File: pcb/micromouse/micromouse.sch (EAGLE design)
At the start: 55 parts, among them J1 Connector_M1, J2 Connector_M2, J4 Programmer

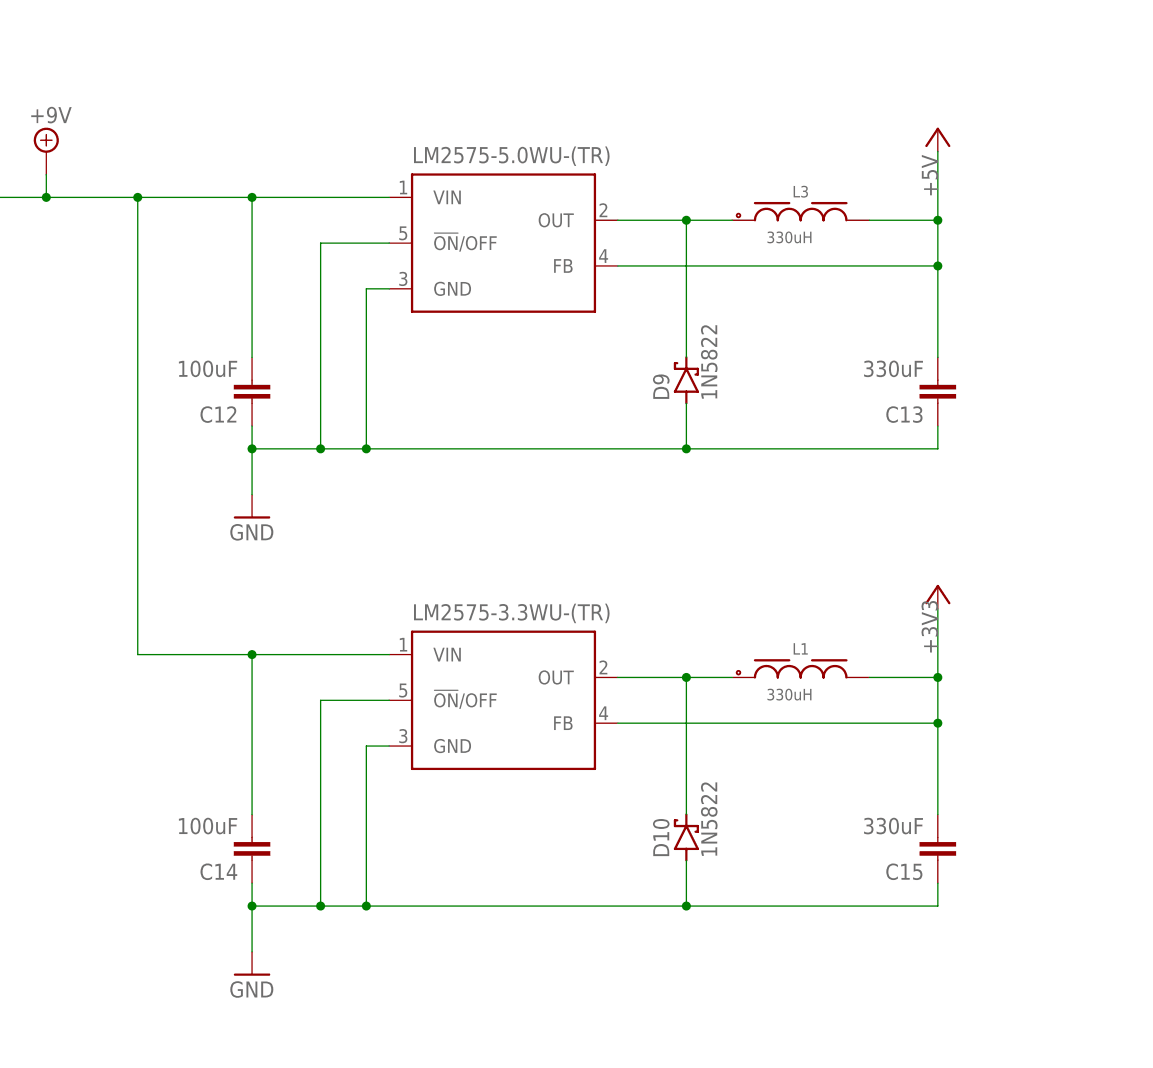
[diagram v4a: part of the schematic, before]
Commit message: Exchanged capacitors and inductances in power supply
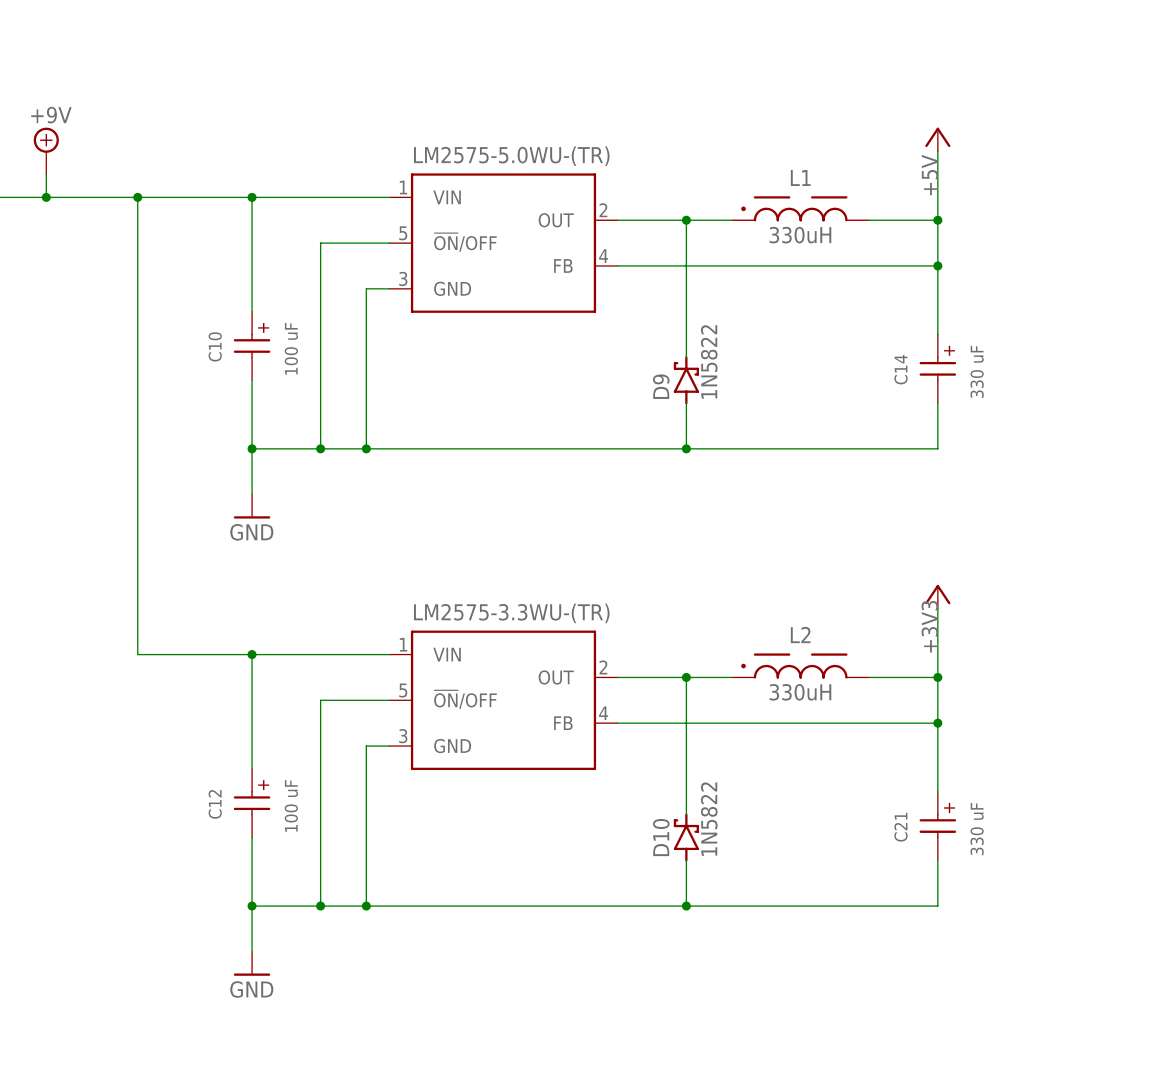
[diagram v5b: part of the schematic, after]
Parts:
- removed C13, C15: 330uF, rcl:C-EUC0805
- removed L3: 330uH, Eagle_WE-PD (rev20a):WE-PD_1210_7447709331
- added C10: 100 uF, Eagle_WCAP-ATG5 (rev21a):WCAP-ATG5_5X11_860020272005
- added C21: 330 uF, Eagle_WCAP-ATG5 (rev21a):WCAP-ATG5_6.3X11_860020273010
- added L2: 330uH, Eagle_WE-TIS (rev22a):WE-TIS_1111_7447471331
- C12: value 100uF -> 100 uF; device rcl:C-EUC1210 -> Eagle_WCAP-ATG5 (rev21a):WCAP-ATG5_5X11_860020272005
- C14: value 100uF -> 330 uF; device rcl:C-EUC1210 -> Eagle_WCAP-ATG5 (rev21a):WCAP-ATG5_6.3X11_860020273010
- L1: device Eagle_WE-PD (rev20a):WE-PD_1210_7447709331 -> Eagle_WE-TIS (rev22a):WE-TIS_1111_7447471331
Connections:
- net +3V3: now also C21.+, L2.2; no longer C15.2, L1.2
- net +5V: now also C14.+, L1.2; no longer C13.2, L3.2
- net +9V: now also C10.+, C12.+; no longer C12.2, C14.2
- net GND: now also C10.-, C12.-, C14.-, C21.-; no longer C12.1, C13.1, C14.1, C15.1
- net N$7: now also L1.1; no longer L3.1
- net N$8: now also L2.1; no longer L1.1
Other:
- moved on the sheet: L1

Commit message: Add test points
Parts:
- added 3V3_TEST, 5V_TEST, 9V_TEST, AVDD_TEST, AVSS_TEST1, GND_TEST, IR0_TEST, IR1_TEST, IR2_TEST, PWM1L1_TEST, PWM1L2_TEST: (no value), wirepad:3,17/1,3
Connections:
- net +3V3: now also 3V3_TEST.P
- net +5V: now also 5V_TEST.P
- net +9V: now also 9V_TEST.P
- net AVDD: now also AVDD_TEST.P
- net AVSS: now also AVSS_TEST1.P
- net GND: now also GND_TEST.P
- net IR0: now also IR0_TEST.P
- net IR1: now also IR1_TEST.P
- net IR2: now also IR2_TEST.P
- net PWM1L1: now also PWM1L1_TEST.P
- net PWM1L2: now also PWM1L2_TEST.P
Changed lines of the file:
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@@
 <part name="L1" library="Eagle_WE-TIS (rev22a)" deviceset="WE-TIS_1111" device="" package3d_urn="urn:adsk.eagle:package:12988462/4" technology="_7447471331" value="330uH"/>
 <part name="L2" library="Eagle_WE-TIS (rev22a)" deviceset="WE-TIS_1111" device="" package3d_urn="urn:adsk.eagle:package:12988462/4" technology="_7447471331" value="330uH"/>
+<part name="9V_TEST" library="wirepad" library_urn="urn:adsk.eagle:library:412" deviceset="3,17/1,3" device="" package3d_urn="urn:adsk.eagle:package:30833/1"/>
+<part name="5V_TEST" library="wirepad" library_urn="urn:adsk.eagle:library:412" deviceset="3,17/1,3" device="" package3d_urn="urn:adsk.eagle:package:30833/1"/>
+<part name="3V3_TEST" library="wirepad" library_urn="urn:adsk.eagle:library:412" deviceset="3,17/1,3" device="" package3d_urn="urn:adsk.eagle:package:30833/1"/>
+<part name="IR0_TEST" library="wirepad" library_urn="urn:adsk.eagle:library:412" deviceset="3,17/1,3" device="" package3d_urn="urn:adsk.eagle:package:30833/1"/>
+<part name="IR1_TEST" library="wirepad" library_urn="urn:adsk.eagle:library:412" deviceset="3,17/1,3" device="" package3d_urn="urn:adsk.eagle:package:30833/1"/>
+<part name="IR2_TEST" library="wirepad" library_urn="urn:adsk.eagle:library:412" deviceset="3,17/1,3" device="" package3d_urn="urn:adsk.eagle:package:30833/1"/>
+<part name="AVDD_TEST" library="wirepad" library_urn="urn:adsk.eagle:library:412" deviceset="3,17/1,3" device="" package3d_urn="urn:adsk.eagle:package:30833/1"/>
+<part name="PWM1L2_TEST" library="wirepad" library_urn="urn:adsk.eagle:library:412" deviceset="3,17/1,3" device="" package3d_urn="urn:adsk.eagle:package:30833/1"/>
+<part name="PWM1L1_TEST" library="wirepad" library_urn="urn:adsk.eagle:library:412" deviceset="3,17/1,3" device="" package3d_urn="urn:adsk.eagle:package:30833/1"/>
+<part name="GND_TEST" library="wirepad" library_urn="urn:adsk.eagle:library:412" deviceset="3,17/1,3" device="" package3d_urn="urn:adsk.eagle:package:30833/1"/>
+<part name="AVSS_TEST1" library="wirepad" library_urn="urn:adsk.eagle:library:412" deviceset="3,17/1,3" device="" package3d_urn="urn:adsk.eagle:package:30833/1"/>
 </parts>
 <sheets>
@@
 <attribute name="NAME" x="10.16" y="295.91" size="1.778" layer="95" align="bottom-center"/>
 <attribute name="VALUE" x="10.16" y="289.56" size="1.778" layer="96" align="bottom-center"/>
+</instance>
+<instance part="9V_TEST" gate="1" x="-73.66" y="342.9" smashed="yes" rot="R90">
+<attribute name="NAME" x="-75.5142" y="334.137" size="1.778" layer="95" rot="R90"/>
+<attribute name="VALUE" x="-70.358" y="341.757" size="1.778" layer="96" rot="R90"/>
+</instance>
+<instance part="5V_TEST" gate="1" x="27.94" y="342.9" smashed="yes" rot="R180">
+<attribute name="NAME" x="36.703" y="341.0458" size="1.778" layer="95" rot="R180"/>
+<attribute name="VALUE" x="29.083" y="346.202" size="1.778" layer="96" rot="R180"/>
+</instance>
+<instance part="3V3_TEST" gate="1" x="27.94" y="292.1" smashed="yes" rot="R180">
+<attribute name="NAME" x="39.243" y="290.2458" size="1.778" layer="95" rot="R180"/>
+<attribute name="VALUE" x="29.083" y="295.402" size="1.778" layer="96" rot="R180"/>
+</instance>
+<instance part="IR0_TEST" gate="1" x="147.32" y="309.88" smashed="yes" rot="R180">
+<attribute name="NAME" x="156.083" y="308.0258" size="1.778" layer="95" rot="R180"/>
+<attribute name="VALUE" x="148.463" y="313.182" size="1.778" layer="96" rot="R180"/>
+</instance>
+<instance part="IR1_TEST" gate="1" x="147.32" y="292.1" smashed="yes" rot="R180">
+<attribute name="NAME" x="156.083" y="290.2458" size="1.778" layer="95" rot="R180"/>
+<attribute name="VALUE" x="148.463" y="295.402" size="1.778" layer="96" rot="R180"/>
+</instance>
+<instance part="IR2_TEST" gate="1" x="147.32" y="274.32" smashed="yes" rot="R180">
+<attribute name="NAME" x="156.083" y="272.4658" size="1.778" layer="95" rot="R180"/>
+<attribute name="VALUE" x="148.463" y="277.622" size="1.778" layer="96" rot="R180"/>
+</instance>
+<instance part="AVDD_TEST" gate="1" x="154.94" y="66.04" smashed="yes" rot="R180">
+<attribute name="NAME" x="163.703" y="64.1858" size="1.778" layer="95" rot="R180"/>
+<attribute name="VALUE" x="156.083" y="69.342" size="1.778" layer="96" rot="R180"/>
+</instance>
+<instance part="PWM1L2_TEST" gate="1" x="58.42" y="134.62" smashed="yes">
+<attribute name="NAME" x="42.037" y="136.4742" size="1.778" layer="95"/>
+<attribute name="VALUE" x="57.277" y="131.318" size="1.778" layer="96"/>
+</instance>
+<instance part="PWM1L1_TEST" gate="1" x="58.42" y="124.46" smashed="yes">
+<attribute name="NAME" x="42.037" y="126.3142" size="1.778" layer="95"/>
+<attribute name="VALUE" x="57.277" y="121.158" size="1.778" layer="96"/>
+</instance>
+<instance part="GND_TEST" gate="1" x="-86.36" y="340.36" smashed="yes" rot="R180">
+<attribute name="NAME" x="-82.677" y="343.5858" size="1.778" layer="95" rot="R180"/>
+<attribute name="VALUE" x="-85.217" y="343.662" size="1.778" layer="96" rot="R180"/>
+</instance>
+<instance part="AVSS_TEST1" gate="1" x="154.94" y="53.34" smashed="yes" rot="R180">
+<attribute name="NAME" x="163.703" y="51.4858" size="1.778" layer="95" rot="R180"/>
+<attribute name="VALUE" x="156.083" y="56.642" size="1.778" layer="96" rot="R180"/>
 </instance>
 </instances>
@@
 <wire x1="-88.9" y1="340.36" x2="-88.9" y2="335.28" width="0.1524" layer="91"/>
 <pinref part="SV5" gate="G$1" pin="1"/>
+<pinref part="GND_TEST" gate="1" pin="P"/>
+<junction x="-88.9" y="340.36"/>
 </segment>
 <segment>
@@
 <pinref part="R14" gate="G$1" pin="2"/>
 <pinref part="C9" gate="G$1" pin="2"/>
+<pinref part="AVDD_TEST" gate="1" pin="P"/>
 </segment>
 </net>
@@
 <junction x="25.4" y="287.02"/>
 <pinref part="L2" gate="G$1" pin="2"/>
+<pinref part="3V3_TEST" gate="1" pin="P"/>
 </segment>
 <segment>
@@
 <pinref part="R13" gate="G$1" pin="2"/>
 <pinref part="C9" gate="G$1" pin="1"/>
+<pinref part="AVSS_TEST1" gate="1" pin="P"/>
 </segment>
 </net>
@@
 <junction x="25.4" y="337.82"/>
 <pinref part="L1" gate="G$1" pin="2"/>
+<pinref part="5V_TEST" gate="1" pin="P"/>
 </segment>
 <segment>
@@
 <wire x1="111.76" y1="274.32" x2="144.78" y2="274.32" width="0.1524" layer="91"/>
 <label x="139.7" y="274.32" size="1.778" layer="95"/>
+<pinref part="IR2_TEST" gate="1" pin="P"/>
 </segment>
 </net>
@@
 <pinref part="C10" gate="G$1" pin="+"/>
 <pinref part="C12" gate="G$1" pin="+"/>
+<pinref part="9V_TEST" gate="1" pin="P"/>
 </segment>
 </net>
@@
 <wire x1="71.12" y1="124.46" x2="60.96" y2="124.46" width="0.1524" layer="91"/>
 <label x="60.96" y="124.46" size="1.778" layer="95"/>
+<pinref part="PWM1L1_TEST" gate="1" pin="P"/>
 </segment>
 <segment>
@@
 <wire x1="71.12" y1="134.62" x2="60.96" y2="134.62" width="0.1524" layer="91"/>
 <label x="60.96" y="134.62" size="1.778" layer="95"/>
+<pinref part="PWM1L2_TEST" gate="1" pin="P"/>
 </segment>
 <segment>
@@
 <wire x1="111.76" y1="309.88" x2="144.78" y2="309.88" width="0.1524" layer="91"/>
 <label x="139.7" y="309.88" size="1.778" layer="95"/>
+<pinref part="IR0_TEST" gate="1" pin="P"/>
 </segment>
 </net>
@@
 <wire x1="111.76" y1="292.1" x2="144.78" y2="292.1" width="0.1524" layer="91"/>
 <label x="139.7" y="292.1" size="1.778" layer="95"/>
-</segment>
-</net>
+<pinref part="IR1_TEST" gate="1" pin="P"/>
+</segment>
+</net>

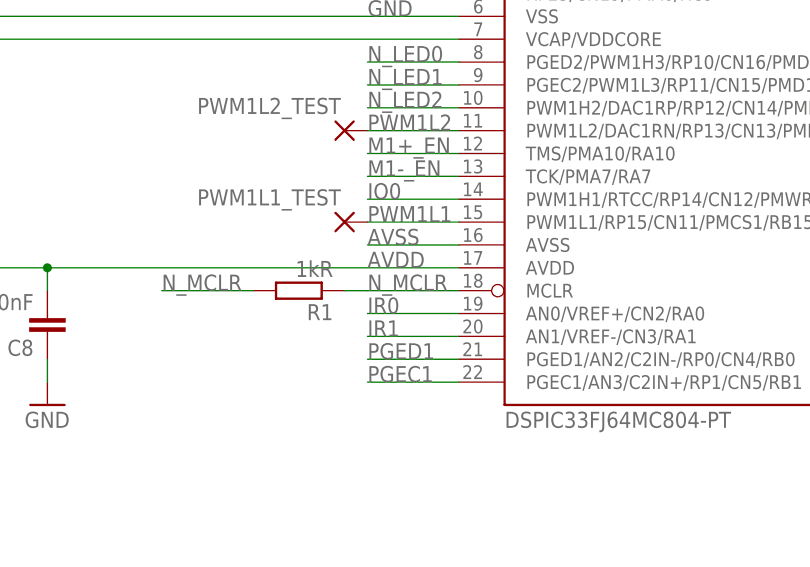
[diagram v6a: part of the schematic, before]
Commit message: Increase width of lanes, all 45 degree angles errors resolved design rules obeyed
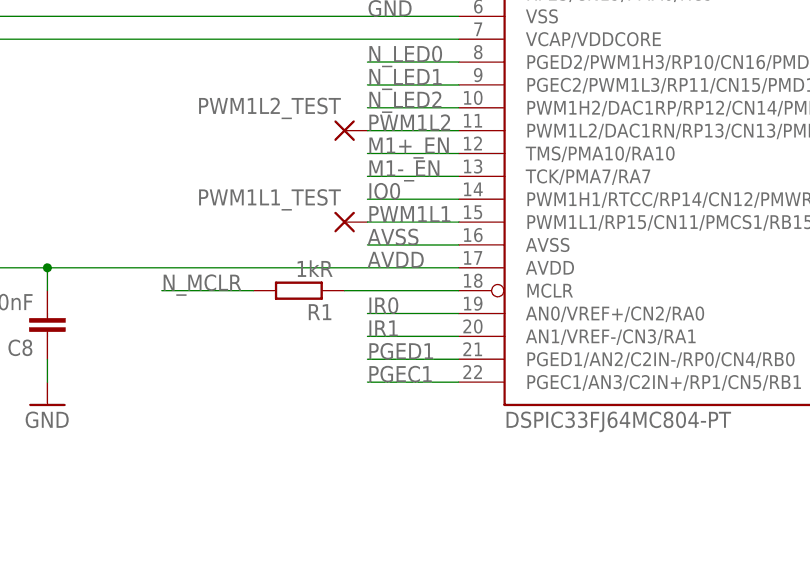
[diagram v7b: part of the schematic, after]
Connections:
- new net N$1: MICROCONTROLLER.MCLR, R1.1
- net N_MCLR: no longer MICROCONTROLLER.MCLR, R1.1
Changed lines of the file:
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@@
-</segment>
-<segment>
-<wire x1="71.12" y1="116.84" x2="63.5" y2="116.84" width="0.1524" layer="91"/>
-<label x="60.96" y="116.84" size="1.778" layer="95"/>
-<pinref part="MICROCONTROLLER" gate="G$1" pin="MCLR"/>
-<pinref part="R1" gate="G$1" pin="1"/>
-<wire x1="63.5" y1="116.84" x2="60.96" y2="116.84" width="0.1524" layer="91"/>
-<wire x1="58.42" y1="116.84" x2="60.96" y2="116.84" width="0.1524" layer="91"/>
 </segment>
 <segment>
@@
 </segment>
 </net>
+<net name="N$1" class="0">
+<segment>
+<pinref part="R1" gate="G$1" pin="1"/>
+<pinref part="MICROCONTROLLER" gate="G$1" pin="MCLR"/>
+<wire x1="58.42" y1="116.84" x2="71.12" y2="116.84" width="0.1524" layer="91"/>
+</segment>
+</net>

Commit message: Renamed parts in ascending order
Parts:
- removed C20: 100nF, rcl:C-EUC0805
- removed C21: 330 uF, Eagle_WCAP-ATG5 (rev21a):WCAP-ATG5_6.3X11_860020273010
- removed LED0: green, led:LEDCHIP-LED0805
- removed R13, R14: 10R, rcl:R-EU_R0805
- added C13: 10uF, rcl:C-EUC0805
- added C15: 100nF, rcl:C-EUC0805
- added LED5: green, led:LEDCHIP-LED0805
- added R2: 1kR, rcl:R-EU_R0805
- added R6: 10kR, rcl:R-EU_R0805
- C1, C2: value 100nF -> 100 uF; device rcl:C-EUC0805 -> Eagle_WCAP-ATG5 (rev21a):WCAP-ATG5_5X11_860020272005
- C10, C12: value 100 uF -> 100nF; device Eagle_WCAP-ATG5 (rev21a):WCAP-ATG5_5X11_860020272005 -> rcl:C-EUC0805
- C14: value 330 uF -> 100nF; device Eagle_WCAP-ATG5 (rev21a):WCAP-ATG5_6.3X11_860020273010 -> rcl:C-EUC0805
- C17, C9: value 10uF -> 100nF
- C3: value 100nF -> 10uF
- C4, C8: value 100nF -> 20pF
- C5, C6: value 20pF -> 330 uF; device rcl:C-EUC0805 -> Eagle_WCAP-ATG5 (rev21a):WCAP-ATG5_6.3X11_860020273010
- IC1: value LM2596S -> LM2575-5.0WU-(TR)
- IC2: value LM2596S -> LM2575-3.3WU-(TR)
- LED1: value green -> Spacing_LED_front; device led:LEDCHIP-LED0805 -> led:LED5MM
- LED2: value green -> Spacing_LED_back; device led:LEDCHIP-LED0805 -> led:LED5MM
- LED3: value Spacing_LED_front -> green; device led:LED5MM -> led:LEDCHIP-LED0805
- LED4: value Spacing_LED_back -> green; device led:LED5MM -> led:LEDCHIP-LED0805
- R1: value 1kR -> 10kR
- R3, R4: value 10kR -> 10R
- SV1: value IR sensor 0 -> Battery connector
- SV2: value IR sensor 1 -> Pin header; device con-lstb:MA03-1 -> con-lstb:MA10-2
- SV3: value IR sensor 2 -> IR sensor 0
- SV4: value Pin header -> IR sensor 1; device con-lstb:MA10-2 -> con-lstb:MA03-1
- SV5: value Battery connector -> IR sensor 2
- renumbered 3V3_TEST to PAD4, 5V_TEST to PAD3, 9V_TEST to PAD2, AVDD_TEST to PAD10, AVSS_TEST1 to PAD11, BTN_1 to S3, BTN_2 to S4, D10 to D2, D9 to D1, GND_TEST to PAD1, H-BRIDGE to IC4, HC05 to SV7, IR0_TEST to PAD7, IR1_TEST to PAD8, IR2_TEST to PAD9, J1 to SV8, J2 to SV9, J4 to SV6, LM2575-3.3WU-(TR) to IC2, LM2575-5.0WU-(TR) to IC1, MICROCONTROLLER to IC3, OSCILLATOR to Y1, PWM1L1_TEST to PAD6, PWM1L2_TEST to PAD5, R10 to R5, R11 to R7, R12 to R9, RESET to S2
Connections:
- net +3V3: now also C14.2, C15.2, C17.2, C6.+, C9.2, R1.2, R3.1, SV2.7; no longer C19.2, C20.2, C21.+, C3.2, C7.2, R14.1, R8.2, SV4.7
- net +5V: now also C10.2, C12.2, C19.2, C5.+, SV5.1; no longer C1.2, C14.+, C2.2, C4.2, SV1.1
- net +9V: now also C1.+, C2.+; no longer C10.+, C12.+
- net AVDD: now also C13.2, C7.2, R3.2; no longer C8.2, C9.2, R14.2
- net AVSS: now also C13.1, R4.2; no longer C9.1, R13.2
- net BTN_1: now also R6.2; no longer R3.2
- net BTN_2: now also R8.2; no longer R4.2
- net GND: now also C1.-, C10.1, C12.1, C14.1, C15.1, C2.-, C5.-, C6.-, C9.1, R6.1, R8.1, SV1.1, SV2.8, SV5.2; no longer C1.1, C10.-, C12.-, C14.-, C2.1, C20.1, C21.-, C5.1, C6.1, R13.1, R3.1, SV1.2, SV4.8, SV5.1
- net IO0: now also SV2.9; no longer SV4.9
- net IO1: now also SV2.11; no longer SV4.11
- net IO2: now also SV2.13; no longer SV4.13
- net IO3: now also SV2.15; no longer SV4.15
- net IO4: now also SV2.16; no longer SV4.16
- net IO5: now also SV2.17; no longer SV4.17
- net IO6: now also SV2.18; no longer SV4.18
- net IO7: now also SV2.19; no longer SV4.19
- net IO8: now also SV2.20; no longer SV4.20
- net IR0: now also SV3.3; no longer SV1.3
- net IR1: now also SV4.3; no longer SV2.3
- net IR2: now also SV5.3; no longer SV3.3
- net N$1: now also R2.1; no longer R1.1
- net N$2: now also SV1.3; no longer SV5.3
- net N$4: now also LED3.A; no longer LED0.A
- net N$5: now also LED4.A; no longer LED1.A
- net N$6: now also LED5.A; no longer LED2.A
- net N_LED0: now also LED3.C, SV2.14; no longer LED0.C, SV4.14
- net N_LED1: now also LED4.C, SV2.12; no longer LED1.C, SV4.12
- net N_LED2: now also LED5.C, SV2.10; no longer LED2.C, SV4.10
- net N_MCLR: now also R1.1, R2.2; no longer R1.2, R8.1
- net OSC1: now also C4.2; no longer C6.2
- net OSC2: now also C8.2; no longer C5.2
- net PWM2H1: now also SV2.6; no longer SV4.6
- net PWM2L1: now also SV2.4; no longer SV4.4
- net RX: now also SV2.3; no longer SV4.3
- net TX: now also SV2.5; no longer SV4.5
- net VCAP/VDDCORE: now also C3.2; no longer C17.2
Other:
- moved on the sheet: C11, C17, C18, C19, C3, C4, C7, C8, C9, LED1, LED2, LED3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
